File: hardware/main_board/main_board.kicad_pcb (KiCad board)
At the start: 4 copper layers, 21.7 x 58 mm, 45 parts, among them P1 USB_OTG, P2 CONN_01X02, Q1 MMBT2222, Q2 MMBT2222, SW1 SW_DPDT_x2, SW2 SW_Push, U1 ESP-12E, U2 CP2104, U3 MCP9808, U4 MMA8451Q, U5 MCP73831/2, U6 AP2112

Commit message: Working on layout
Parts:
- removed D4: MBR120, footprint:SOD-123FL
- removed P2: CONN_01X02, footprint:S2B-PH-SM4-TB(LF)(SN)
- removed Q2: MMBT2222, TO_SOT_Packages_SMD:SOT-23
- removed R12, R14, R18, R19, R20: 10k, Resistors_SMD:R_0603
- removed R13, R16: 1k, Resistors_SMD:R_0603
- removed R15: 1M, Resistors_SMD:R_0603
- removed R17: 220k, Resistors_SMD:R_0603
- removed SW2: SW_Push, footprint:KMR7
- removed U6: AP2112, TO_SOT_Packages_SMD:SOT-23-5
- added C10: 0.1u, Capacitors_SMD:C_0603, F.Cu at (151.9, 135.4)
- added J1: eConn_02x03_Odd_Even, Socket_Strips:Socket_Strip_Angled_2x03_Pitch2.54mm, B.Cu at (135.4, 72.9)
- C1, C3, C8: value 1u -> 10u; footprint Capacitors_SMD:C_0603 -> Capacitors_SMD:C_0805
- C2: value 0.1u -> 10u; footprint Capacitors_SMD:C_0603 -> Capacitors_SMD:C_0805
- C4: value 0.1u -> 1u
- C5, C7: value 10u -> 0.1u; footprint Capacitors_SMD:C_0805 -> Capacitors_SMD:C_0603
- C6: value 10u -> 1u; footprint Capacitors_SMD:C_0805 -> Capacitors_SMD:C_0603
- C9: value 1u -> 0.1u
- D1: value LED -> ORG
- D2: value LED -> MBR120; footprint LEDs:LED_0603 -> footprint:SOD-123FL
- D3: value MBR120 -> RED; footprint footprint:SOD-123FL -> LEDs:LED_0603
- P1: value USB_OTG -> CONN_01X02; footprint footprint:10118192 -> footprint:S2B-PH-SM4-TB(LF)(SN)
- Q1: value MMBT2222 -> DMG3415U
- R1: value 1k -> 100k
- R2, R3: value 10k -> 1k
- R4: value 10k -> 1M
- R5: value 10k -> 220k
- R6: value 4.7k -> 10k
- R8: value 24k -> 15k
- R9: value 47k -> 10k
- SW1: moved to F.Cu
- U1: value ESP-12E -> MCP73831/2; footprint footprint:ESP-12E -> TO_SOT_Packages_SMD:SOT-23-5
- U2: value CP2104 -> AP2112; footprint Housings_DFN_QFN:QFN-24-1EP_4x4mm_Pitch0.5mm -> TO_SOT_Packages_SMD:SOT-23-5
- U4: value MMA8451Q -> ESP-WROOM-32D; footprint footprint:MMA8451Q -> footprint:ESP32-WROOM
- U5: value MCP73831/2 -> MMA8451Q; footprint TO_SOT_Packages_SMD:SOT-23-5 -> footprint:MMA8451Q
- moved R9 77.6 mm to (164.6, 137.2), turned to 0 degrees
- moved R8 74.7 mm to (164.8, 134.6), turned to 0 degrees
- moved D3 74.6 mm to (150.9, 137.7), turned to 0 degrees
- moved C6 70.2 mm to (138.7, 137.4), turned to 0 degrees
- moved C9 69.3 mm to (147.3, 137.7)
- moved C5 68.0 mm to (138.7, 134.9), turned to 0 degrees
- moved R11 64.1 mm to (158.2, 139.7), turned to 0 degrees
- moved SW1 63.0 mm to (147.0, 125.6)
- moved U2 62.9 mm to (143.1, 133.7), turned to 0 degrees
- moved C7 62.7 mm to (142.2, 137.7), turned to 0 degrees
- moved P1 62.3 mm to (160.2, 118.4), turned to 0 degrees
- moved C1 61.6 mm to (134.1, 132.3)
- moved C8 61.0 mm to (147.8, 135.1), turned to 0 degrees
- moved U5 60.9 mm to (153.2, 131.1), turned to 0 degrees
- moved C3 60.8 mm to (133.6, 137.9)
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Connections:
- C1 pad 1: Net-(C1-Pad1) -> /VIN
- C2 pad 1: +3V3 -> +BATT
- C4 pad 1: Net-(C4-Pad1) -> +3V3
- C5 pad 1: +BATT -> /RESET
- C6 pad 1: /VIN -> +3V3
- C7 pad 1: +3V3 -> Net-(C7-Pad1)
- C9 pad 1: +5V -> +3V3
- D2 pad 1: Net-(D2-Pad1) -> /VIN
- D2 pad 2: +3V3 -> +5V
- D3 pad 1: /VIN -> GND
- D3 pad 2: +BATT -> Net-(D3-Pad2)
- P1 pad 1: +5V -> +BATT
- P1 pad 2: /USB_D- -> GND
- Q1 pad 1: Net-(Q1-Pad1) -> +5V
- Q1 pad 2: /DTR -> (no net)
- Q1 pad 3: /GPIO0 -> +BATT
- R1 pad 1: /RESET -> GND
- R1 pad 2: /GPIO16 -> +5V
- R10 pad 1: Net-(Q1-Pad1) -> /SDA
- R10 pad 2: /RTS -> +3V3
- R11 pad 1: Net-(Q2-Pad1) -> +3V3
- R11 pad 2: /DTR -> /RESET
- R2 pad 1: /GPIO2 -> Net-(R2-Pad1)
- R2 pad 2: +3V3 -> Net-(D1-Pad1)
- R3 pad 1: /CH_PD -> Net-(D3-Pad2)
- R3 pad 2: +3V3 -> /LED
- R4 pad 1: /GPIO5/SCL -> +BATT
- R4 pad 2: +3V3 -> /BAT_SENSE
- R5 pad 1: /GPIO4/SDA -> /BAT_SENSE
- R5 pad 2: +3V3 -> GND
- R6 pad 2: /GPIO15 -> Net-(R6-Pad2)
- R7 pad 1: /RXD -> /5V_SENSE
- R7 pad 2: +3V3 -> +5V
- R8 pad 1: /GPIO14/SCK -> GND
- R8 pad 2: +5V -> /5V_SENSE
- R9 pad 1: /GPIO14/SCK -> /SCL
- R9 pad 2: GND -> +3V3
- SW1 pad 3: Net-(SW1-Pad3) -> (no net)
- SW1 pad 4: Net-(SW1-Pad4) -> (no net)
- SW1 pad 5: Net-(SW1-Pad5) -> (no net)
- SW1 pad 6: Net-(SW1-Pad6) -> (no net)
- U1 pad 1: /RESET -> Net-(R2-Pad1)
- U1 pad 2: /ADC -> GND
- U1 pad 3: /CH_PD -> +BATT
- U1 pad 4: /GPIO16 -> +5V
- U1 pad 5: /GPIO14/SCK -> Net-(R6-Pad2)
- U2 pad 1: Net-(U2-Pad1) -> /VIN
- U2 pad 3: /USB_D+ -> Net-(SW1-Pad1)
- U2 pad 4: /USB_D- -> (no net)
- U2 pad 5: Net-(C1-Pad1) -> +3V3
- U3 pad 1: /GPIO4/SDA -> /SDA
- U3 pad 2: /GPIO5/SCL -> /SCL
- U3 pad 3: Net-(U3-Pad3) -> (no net)
- U4 pad 1: +3V3 -> GND
- U4 pad 10: GND -> (no net)
- U4 pad 11: Net-(U4-Pad11) -> (no net)
- U4 pad 12: GND -> (no net)
- U4 pad 13: Net-(U4-Pad13) -> (no net)
- U4 pad 14: +3V3 -> (no net)
- U4 pad 15: Net-(U4-Pad15) -> GND
- U4 pad 16: Net-(U4-Pad16) -> /LED
- U4 pad 2: Net-(C4-Pad1) -> +3V3
- U4 pad 3: Net-(U4-Pad3) -> /RESET
- U4 pad 4: /GPIO5/SCL -> (no net)
- U4 pad 5: GND -> (no net)
- U4 pad 6: /GPIO4/SDA -> /5V_SENSE
- U4 pad 7: +3V3 -> /BAT_SENSE
- U4 pad 8: Net-(U4-Pad8) -> (no net)
- U4 pad 9: Net-(U4-Pad9) -> (no net)
- U5 pad 1: Net-(R13-Pad1) -> +3V3
- U5 pad 2: GND -> Net-(C7-Pad1)
- U5 pad 3: +BATT -> (no net)
- U5 pad 4: +5V -> /SCL
- U5 pad 5: Net-(R12-Pad2) -> GND
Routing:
- net /RESET: track 63.8 -> 0.00 mm, vias 6 -> 0
- net /TXD: track 43.8 -> 0.00 mm, vias 3 -> 0
- net /GPIO14/SCK: track 40.3 -> 0.00 mm, vias 2 -> 0
- net /RXD: track 36.3 -> 0.00 mm, vias 3 -> 0
- net +5V: track 33.6 -> 0.00 mm, vias 3 -> 0
- net /GPIO5/SCL: track 33.1 -> 0.00 mm, vias 2 -> 0
- net +BATT: track 31.7 -> 0.00 mm, vias 4 -> 0
- net /GPIO4/SDA: track 31.1 -> 0.00 mm, vias 2 -> 0
- net /GPIO0: track 30.8 -> 0.00 mm, vias 2 -> 0
- net GND: track 28.4 -> 0.00 mm, vias 32 -> 0
- net +3V3: track 25.5 -> 0.00 mm, vias 15 -> 0
- net /VIN: track 25.0 -> 0.00 mm, vias 3 -> 0
- net /ADC: track 22.0 -> 0.00 mm
- net /CH_PD: track 17.6 -> 0.00 mm, vias 2 -> 0
- net /GPIO16: track 17.4 -> 0.00 mm, vias 2 -> 0
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
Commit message: Working on layout
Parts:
- moved U4 1.09 mm to (138.0, 103.0)
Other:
- outline, holes or cut-outs redrawn
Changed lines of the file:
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@@
   )
   (module footprint:ESP32-WROOM (layer F.Cu)
-    (at 138 101.91)
+    (at 138 103)
     (fp_text reference U4 (at -11.557 9.017) (layer F.SilkS)
       (effects (font (size 1 1) (thickness 0.15)))
@@
       (effects (font (size 1 1) (thickness 0.15)))
     )
-    (fp_circle (center 9.906 6.604) (end 10.033 6.858) (layer F.SilkS) (width 0.5))
     (fp_line (start -9 6.75) (end 9 6.75) (layer F.SilkS) (width 0.15))
     (fp_line (start 9 12.75) (end 9 -12.75) (layer F.SilkS) (width 0.15))
@@
   (gr_line (start 131.4 60.2) (end 144.6 60.2) (layer Edge.Cuts) (width 0.1))
   (gr_line (start 128.5 65.65) (end 128.5 59.6) (layer Edge.Cuts) (width 0.1))
-  (gr_line (start 147.5 104.4) (end 147.5 72.35) (layer Edge.Cuts) (width 0.1))
-  (gr_line (start 128.5 104.4) (end 128.5 72.35) (layer Edge.Cuts) (width 0.1))
+  (gr_line (start 147.9 104.4) (end 147.9 72.35) (layer Edge.Cuts) (width 0.1))
+  (gr_line (start 128.1 104.4) (end 128.1 72.35) (layer Edge.Cuts) (width 0.1))
   (gr_line (start 127.15 67) (end 128.5 65.65) (layer Edge.Cuts) (width 0.1))
   (gr_line (start 148.85 67) (end 147.5 65.65) (layer Edge.Cuts) (width 0.1))

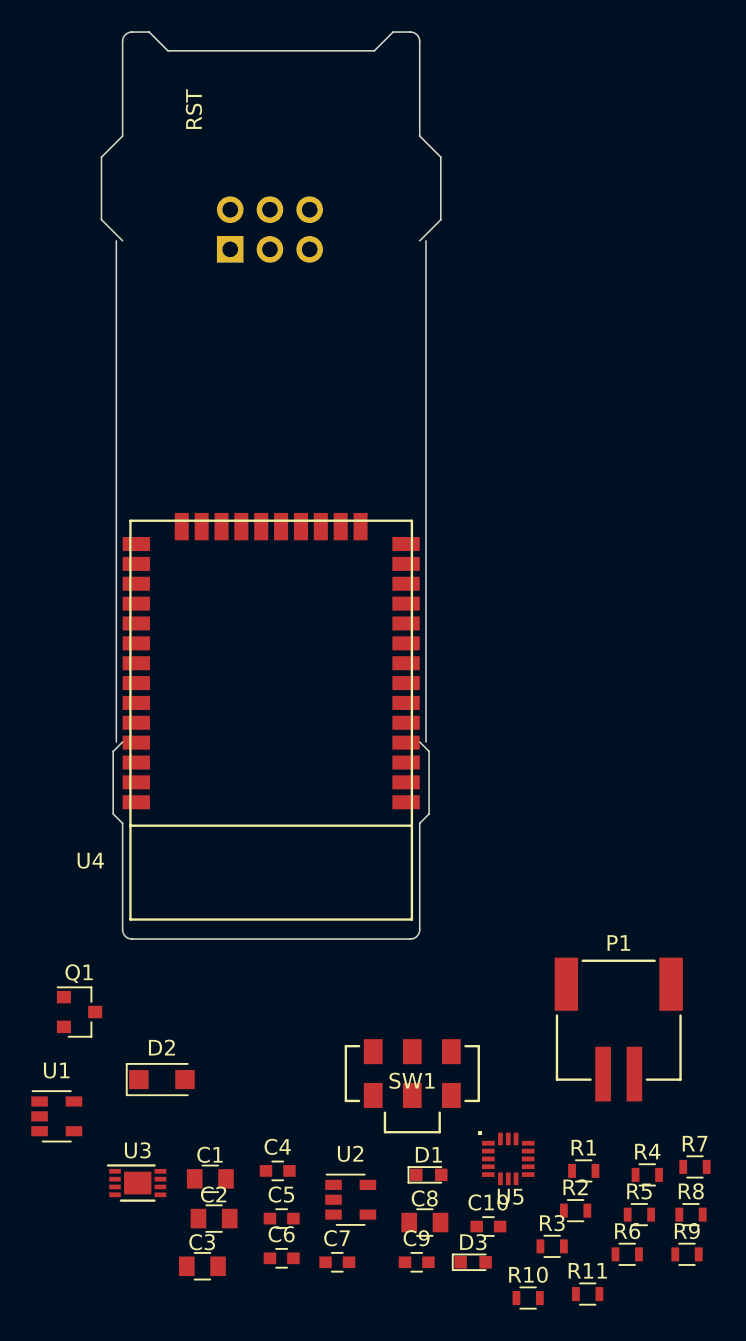
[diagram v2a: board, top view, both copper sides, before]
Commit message: Changed board size to use with new tubes
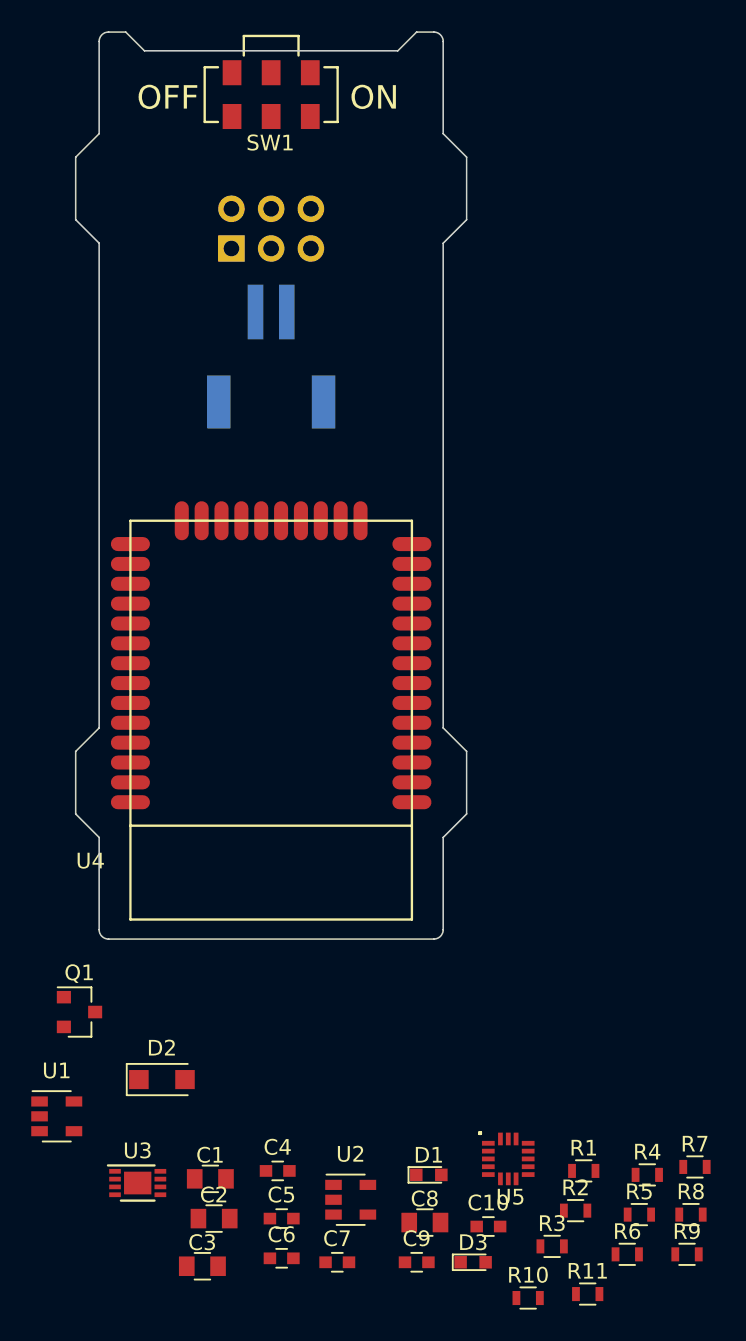
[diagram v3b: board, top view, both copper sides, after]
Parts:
- P1: moved to B.Cu
- moved SW1 63.2 mm to (138.0, 63.0), turned to 180 degrees
- moved P1 40.8 mm to (138.0, 84.2)
- moved J1 0.10 mm to (135.5, 72.8)
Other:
- board size 21.7 x 58 mm -> 25 x 58 mm
- board text removed: "RST"

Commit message: Working on layout
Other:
- net class Default: clearance 0.14 -> 0.1524; trace_width 0.14 -> 0.1524; via_dia 0.36 -> 0.452; via_drill 0.26 -> 0.3
- rule trace_clearance: 0.14 -> 0.1524
- rule trace_min: 0.127 -> 0.1524
- rule via_min_drill: 0.254 -> 0.3
- rule via_min_size: 0.3556 -> 0.452
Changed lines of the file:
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@@
     (no_connects 81)
     (area 125.449999 58.949999 150.550001 117.050001)
-    (thickness 1.6)
+    (thickness 1.2)
     (drawings 31)
     (tracks 0)
@@
   (layers
     (0 F.Cu signal)
-    (1 In1.Cu signal hide)
+    (1 In1.Cu signal)
     (2 In2.Cu signal)
     (31 B.Cu signal)
-    (34 B.Paste user hide)
-    (35 F.Paste user hide)
+    (34 B.Paste user)
+    (35 F.Paste user)
     (36 B.SilkS user)
     (37 F.SilkS user)
-    (38 B.Mask user hide)
-    (39 F.Mask user hide)
+    (38 B.Mask user)
+    (39 F.Mask user)
     (44 Edge.Cuts user)
-    (46 B.CrtYd user hide)
-    (47 F.CrtYd user hide)
+    (46 B.CrtYd user)
+    (47 F.CrtYd user)
   )
   (setup
-    (last_trace_width 0.14)
+    (last_trace_width 0.1524)
     (user_trace_width 0.2)
     (user_trace_width 0.3)
-    (trace_clearance 0.14)
+    (trace_clearance 0.1524)
     (zone_clearance 0.2)
     (zone_45_only no)
-    (trace_min 0.127)
+    (trace_min 0.1524)
     (segment_width 0.2)
     (edge_width 0.1)
-    (via_size 0.36)
-    (via_drill 0.26)
-    (via_min_size 0.3556)
-    (via_min_drill 0.254)
-    (user_via 0.48 0.26)
-    (uvia_size 0.36)
-    (uvia_drill 0.26)
+    (via_size 0.452)
+    (via_drill 0.3)
+    (via_min_size 0.452)
+    (via_min_drill 0.3)
+    (user_via 0.452 0.3)
+    (uvia_size 0.452)
+    (uvia_drill 0.3)
     (uvias_allowed no)
-    (uvia_min_size 0.3556)
-    (uvia_min_drill 0.254)
+    (uvia_min_size 0.452)
+    (uvia_min_drill 0.3)
     (pcb_text_width 0.3)
     (pcb_text_size 1.5 1.5)
@@
   (net 21 /SDA)
   (net_class Default "This is the default net class."
-    (clearance 0.14)
-    (trace_width 0.14)
-    (via_dia 0.36)
-    (via_drill 0.26)
-    (uvia_dia 0.36)
-    (uvia_drill 0.26)
+    (clearance 0.1524)
+    (trace_width 0.1524)
+    (via_dia 0.452)
+    (via_drill 0.3)
+    (uvia_dia 0.452)
+    (uvia_drill 0.3)
     (add_net +3V3)
     (add_net +5V)
